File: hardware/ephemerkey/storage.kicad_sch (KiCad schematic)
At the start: 2 parts, among them U7 M24M02E

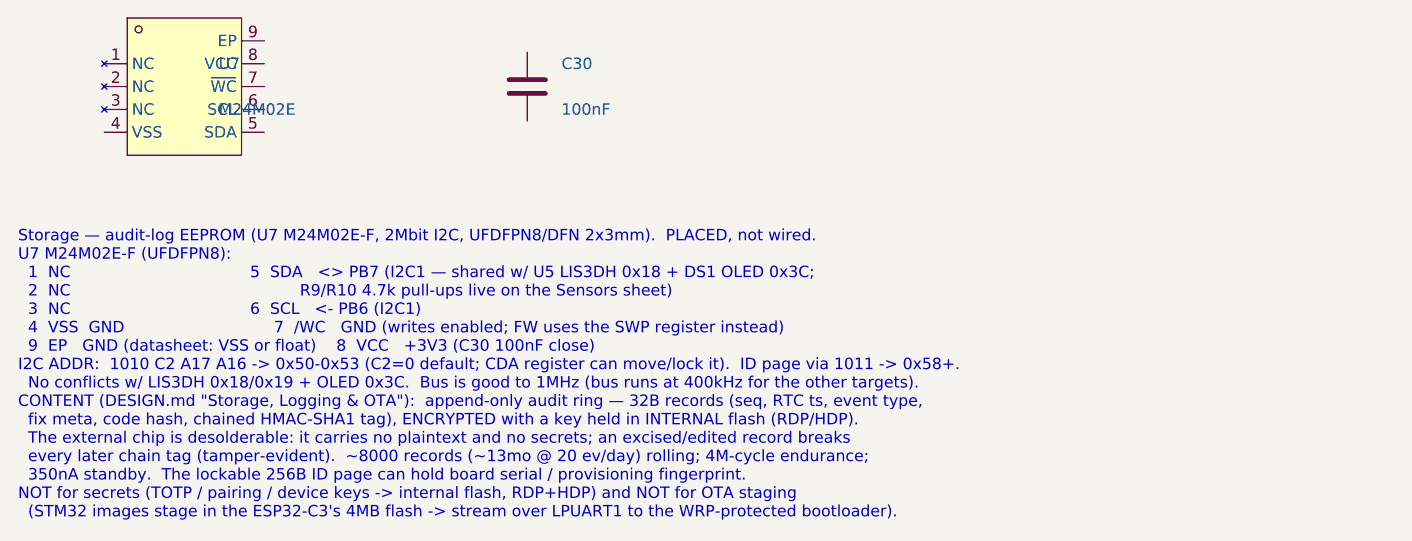
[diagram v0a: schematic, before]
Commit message: hardware+fw: add MAX17048 fuel gauge (U8, I2C1 @0x36) to the PSU sheet
MAX17048G+T10 (LCSC C2682616, TDFN-8 2x2 + EP): 1S ModelGauge SoC monitor,
3uA hibernate, riding the existing I2C1 bus - zero new MCU pins. CELL/VDD
sense at BAT+ (the cell terminal, not VSYS); C31 100nF bypass; CTG/QSTRT/
EP to GND; /ALRT unrouted (no spare pin - firmware polls; alert register
still usable). SDA/SCL logic is independent of VDD, so the 3V3 bus vs a
fading BAT+ is fine.

- Symbol authored into lib/symbols/ephemerkey.kicad_sym from the ADI
  datasheet pin table, cross-checked pin-for-pin against the independently
  authored notchdeck:MAX17048 (sibling project; identical map, same stdlib
  TDFN-8-1EP_2x2mm_P0.5mm_EP0.8x1.2mm footprint). Shared caveat recorded:
  verify EP land vs ADI 21-0168 before fab.
- psu.kicad_sch: surgical splice (sheet is hand-wired; no regen): embedded
  lib symbol, U8 + C31 instances placed near J4, note block updated with
  full pin map + wiring guidance. Property text offsets fixed to be
  relative to the new bodies (KiCad stores them absolute). Render-verified.
- Bus enumerations updated (mcu/sensors/storage notes, manifest + sheets):
  I2C1 = U5 0x18 + DS1 0x3C + U7 0x50-53 + U8 0x36.
- PARTS.md, DESIGN.md (pin table, peripheral summary, BOM).
- ephemerkey-rs: sensors task probes MAX17048 VERSION alongside LIS3DH
  WHO_AM_I; VCELL/SOC register consts staged.

Co-Authored-By: Claude Fable 5 <noreply@anthropic.com>
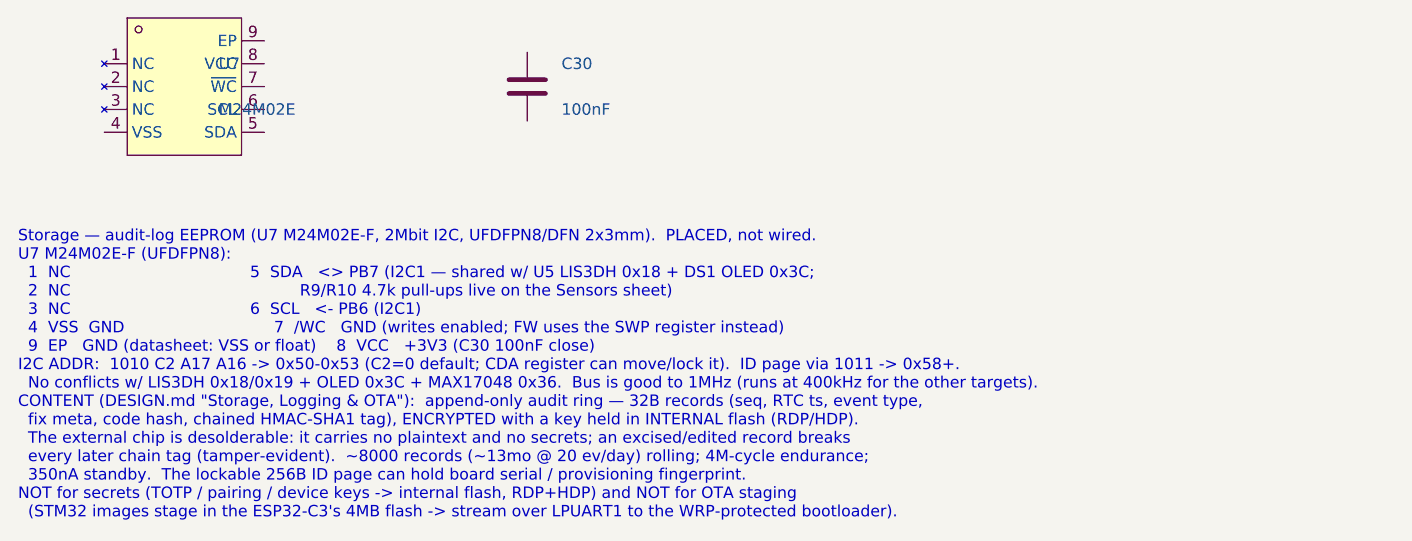
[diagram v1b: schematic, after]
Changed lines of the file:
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@@
 		)
 	)
-	(text "Storage — audit-log EEPROM (U7 M24M02E-F, 2Mbit I2C, UFDFPN8/DFN 2x3mm).  PLACED, not wired.\nU7 M24M02E-F (UFDFPN8):\n  1  NC                                    5  SDA   <> PB7 (I2C1 — shared w/ U5 LIS3DH 0x18 + DS1 OLED 0x3C;\n  2  NC                                              R9/R10 4.7k pull-ups live on the Sensors sheet)\n  3  NC                                    6  SCL   <- PB6 (I2C1)\n  4  VSS  GND                              7  /WC   GND (writes enabled; FW uses the SWP register instead)\n  9  EP   GND (datasheet: VSS or float)    8  VCC   +3V3 (C30 100nF close)\nI2C ADDR:  1010 C2 A17 A16 -> 0x50-0x53 (C2=0 default; CDA register can move/lock it).  ID page via 1011 -> 0x58+.\n  No conflicts w/ LIS3DH 0x18/0x19 + OLED 0x3C.  Bus is good to 1MHz (bus runs at 400kHz for the other targets).\nCONTENT (DESIGN.md \"Storage, Logging & OTA\"):  append-only audit ring — 32B records (seq, RTC ts, event type,\n  fix meta, code hash, chained HMAC-SHA1 tag), ENCRYPTED with a key held in INTERNAL flash (RDP/HDP).\n  The external chip is desolderable: it carries no plaintext and no secrets; an excised/edited record breaks\n  every later chain tag (tamper-evident).  ~8000 records (~13mo @ 20 ev/day) rolling; 4M-cycle endurance;\n  350nA standby.  The lockable 256B ID page can hold board serial / provisioning fingerprint.\nNOT for secrets (TOTP / pairing / device keys -> internal flash, RDP+HDP) and NOT for OTA staging\n  (STM32 images stage in the ESP32-C3's 4MB flash -> stream over LPUART1 to the WRP-protected bootloader)."
+	(text "Storage — audit-log EEPROM (U7 M24M02E-F, 2Mbit I2C, UFDFPN8/DFN 2x3mm).  PLACED, not wired.\nU7 M24M02E-F (UFDFPN8):\n  1  NC                                    5  SDA   <> PB7 (I2C1 — shared w/ U5 LIS3DH 0x18 + DS1 OLED 0x3C;\n  2  NC                                              R9/R10 4.7k pull-ups live on the Sensors sheet)\n  3  NC                                    6  SCL   <- PB6 (I2C1)\n  4  VSS  GND                              7  /WC   GND (writes enabled; FW uses the SWP register instead)\n  9  EP   GND (datasheet: VSS or float)    8  VCC   +3V3 (C30 100nF close)\nI2C ADDR:  1010 C2 A17 A16 -> 0x50-0x53 (C2=0 default; CDA register can move/lock it).  ID page via 1011 -> 0x58+.\n  No conflicts w/ LIS3DH 0x18/0x19 + OLED 0x3C + MAX17048 0x36.  Bus is good to 1MHz (runs at 400kHz for the other targets).\nCONTENT (DESIGN.md \"Storage, Logging & OTA\"):  append-only audit ring — 32B records (seq, RTC ts, event type,\n  fix meta, code hash, chained HMAC-SHA1 tag), ENCRYPTED with a key held in INTERNAL flash (RDP/HDP).\n  The external chip is desolderable: it carries no plaintext and no secrets; an excised/edited record breaks\n  every later chain tag (tamper-evident).  ~8000 records (~13mo @ 20 ev/day) rolling; 4M-cycle endurance;\n  350nA standby.  The lockable 256B ID page can hold board serial / provisioning fingerprint.\nNOT for secrets (TOTP / pairing / device keys -> internal flash, RDP+HDP) and NOT for OTA staging\n  (STM32 images stage in the ESP32-C3's 4MB flash -> stream over LPUART1 to the WRP-protected bootloader)."
 		(exclude_from_sim no)
 		(at 12.00 56.64 0)
